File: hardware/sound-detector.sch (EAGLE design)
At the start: 42 parts, among them IC1 LMV324, J1 GATORGATOR_MINI, J2 GATORGATOR_MINI, J3 GATORGATOR_MINI, J4 GATORGATOR_MINI, J5 GATORGATOR_MINI

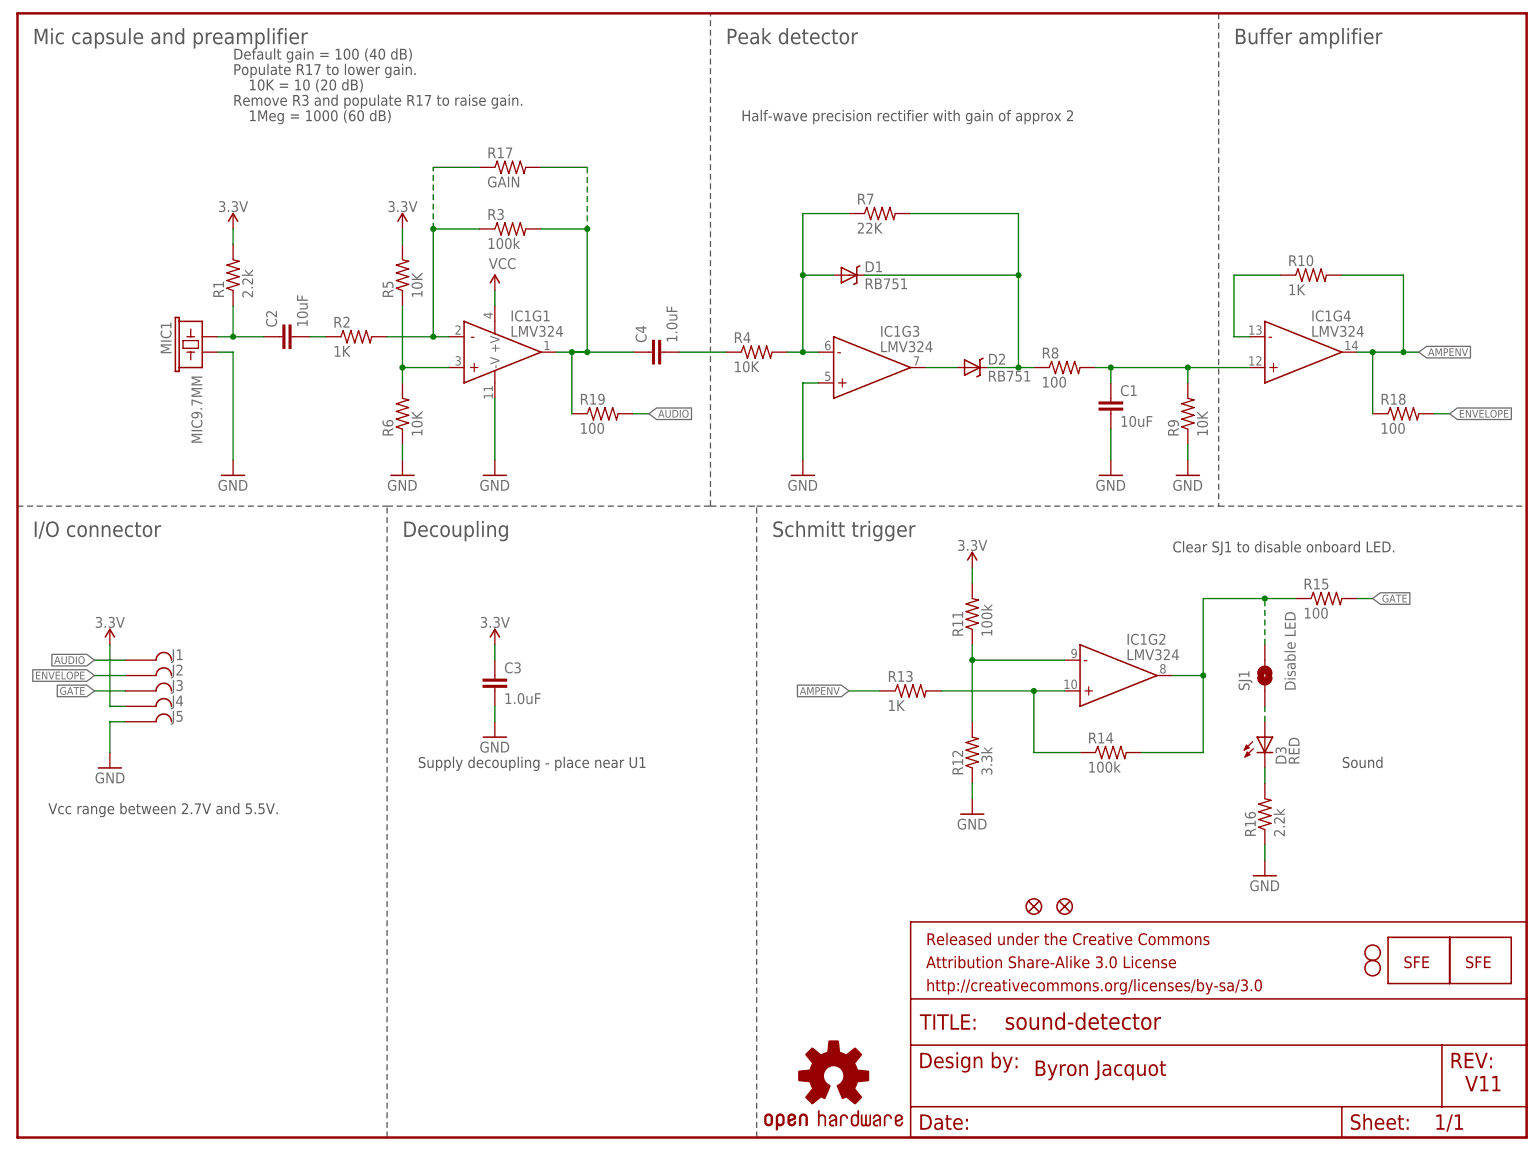
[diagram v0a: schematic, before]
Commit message: adding protection circuitry
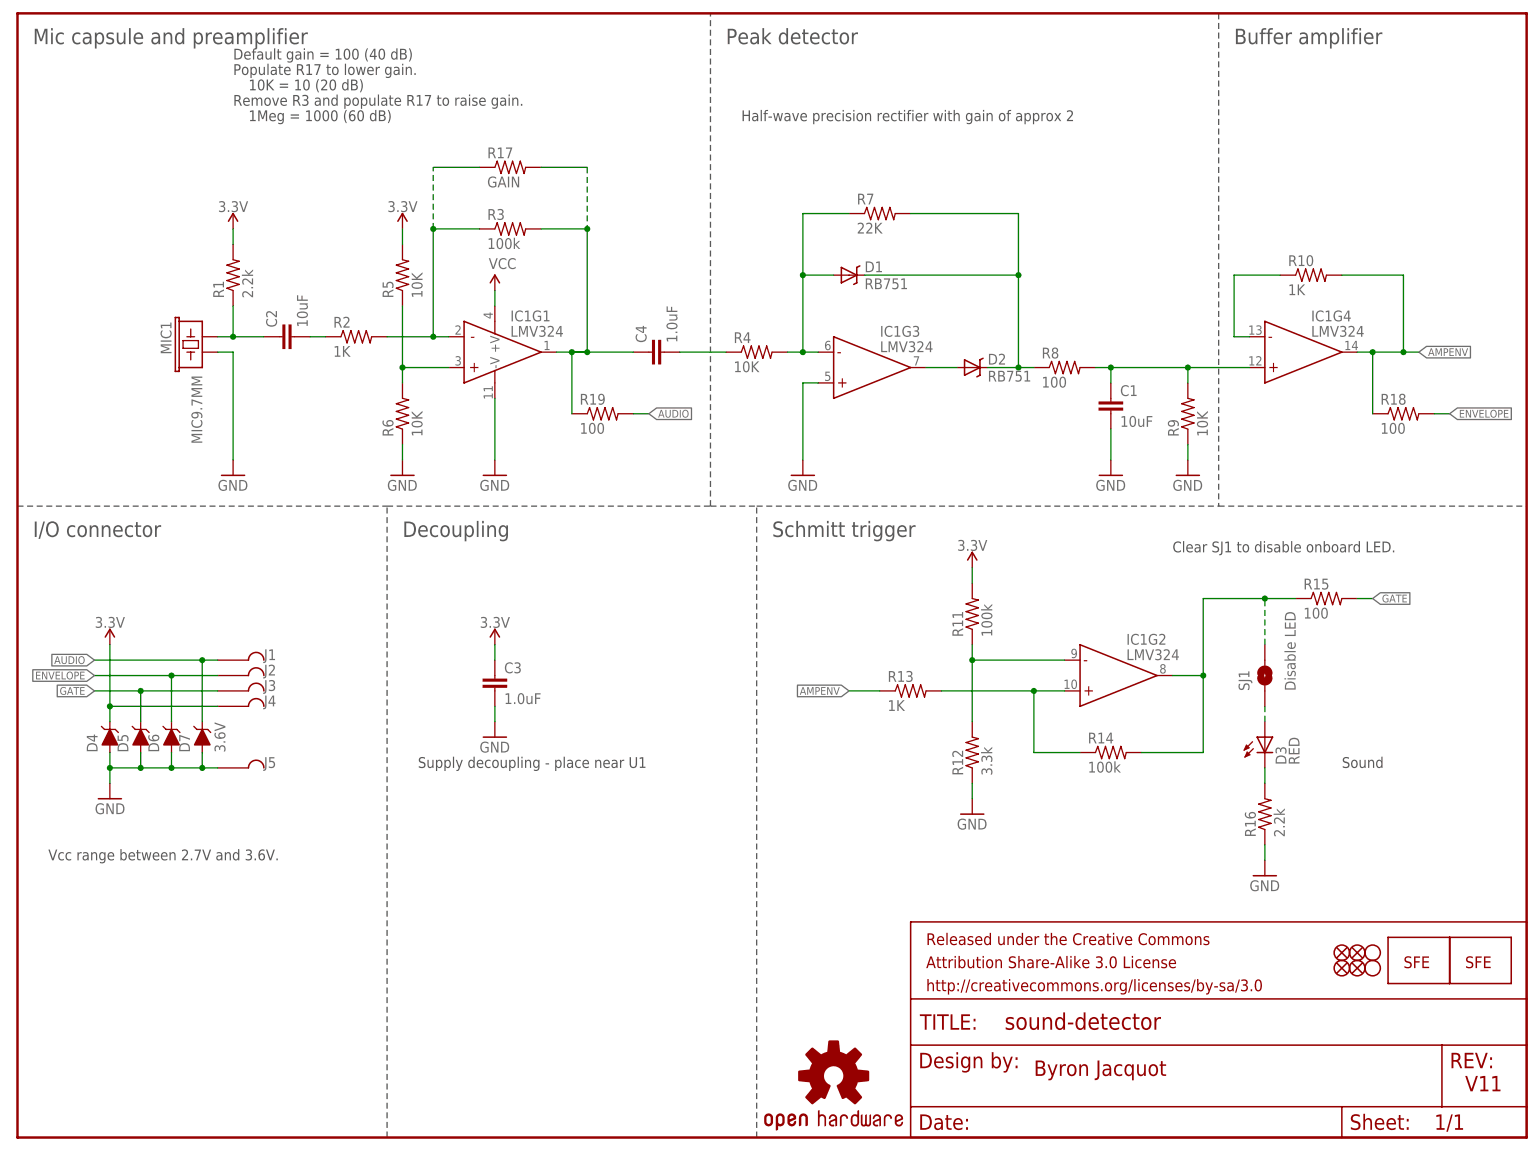
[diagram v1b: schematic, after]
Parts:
- added D4, D5, D6, D7: 3.6V, SparkFun-DiscreteSemi:DIODE-ZENER-BZT52C3V6S
- added FID1, FID2: FIDUCIAL1X2, SparkFun-Aesthetics:FIDUCIAL1X2
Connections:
- net 3.3V: now also D4.C
- net AUDIO: now also D7.C
- net ENVELOPE: now also D6.C
- net GATE: now also D5.C
- net GND: now also D4.A, D5.A, D6.A, D7.A
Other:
- note added: "Vcc range between 2.7V and 3.6V."
- note removed: "Vcc range between 2.7V and 5.5V."
- moved on the sheet: J1, J2, J3, J4, J5

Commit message: initial layout
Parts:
- removed D7: 3.6V, SparkFun-DiscreteSemi:DIODE-ZENER-BZT52C3V6S
- removed SJ1: Disable LED, SparkFun-Passives:SOLDERJUMPERNC
- removed STANDOFF1, STANDOFF2: STAND-OFF, SparkFun-Electromechanical:STAND-OFF
- added J6, J7, J8: GATORGATOR_MINI, SparkFun-Connectors:GATORGATOR_MINI
- added Q1: 2.5A/30V/105mΩ, SparkFun-DiscreteSemi:MOSFET_PCH-DMG2307L
- added R20: 1M, SparkFun-Resistors:1MOHM-0603-1/4W-5%
- added R21, R22, R23: 10k, SparkFun-Resistors:10KOHM-0603-1/10W-1%
- added S1: (no value), SparkFun-Switches:SWITCH-SP3T-SMD
- added U1: ADS1015, SparkFun-IC-Conversion:ADS1015
- C3, C4: device SparkFun-Capacitors:1.0UF-16V-10%(0603) -> SparkFun-Capacitors:1.0UF-0603-16V-10%
- D1, D2: value RB751 -> 120mA/40V/370mV; device SparkFun-DiscreteSemi:RB751 -> SparkFun-DiscreteSemi:DIODE-SCHOTTKY-RB751S40
- LOGO1: value OSHW-LOGOM -> OSHW-LOGOS; device SparkFun-Aesthetics:OSHW-LOGOM -> SparkFun-Aesthetics:OSHW-LOGOS
- LOGO2: value LOGO-SFENW2 -> SFE_LOGO_NAME_FLAME.2_INCH; device SparkFun-Aesthetics:LOGO-SFENW2 -> SparkFun-Aesthetics:SFE_LOGO_NAME_FLAME.2_INCH
- LOGO3: value LOGO-SFESK -> SFE_LOGO_FLAME.2_INCH; device SparkFun-Aesthetics:LOGO-SFESK -> SparkFun-Aesthetics:SFE_LOGO_FLAME.2_INCH
- R1: device SparkFun-Resistors:2.2KOHM1/10W1%(0603) -> SparkFun-Resistors:2.2KOHM-0603-1/10W-1%
- R10, R13, R2: value 1K -> 1k; device SparkFun-Resistors:1KOHM1/10W1%(0603) -> SparkFun-Resistors:1KOHM-0603-1/10W-1%
- R11, R14, R3: device SparkFun-Resistors:100KOHM1/10W1%(0603) -> SparkFun-Resistors:100KOHM-0603-1/10W-1%
- R15, R18, R19, R8: device SparkFun-Resistors:100OHM1/10W1%(0603) -> SparkFun-Resistors:100OHM-0603-1/4W-5%
- R16: value 2.2k -> 1k; device SparkFun-Resistors:2.2KOHM1/10W1%(0603) -> SparkFun-Resistors:1KOHM-0603-1/10W-1%
- R17: value GAIN -> 10k; device SparkFun-Resistors:RESISTORPTH-1/4W-VERT-KIT -> SparkFun-Resistors:10KOHM-0603-1/10W-1%
- R4, R5, R6, R9: value 10K -> 10k; device SparkFun-Resistors:10KOHM1/10W1%(0603)0603 -> SparkFun-Resistors:10KOHM-0603-1/10W-1%
- R7: value 22K -> 22k; device SparkFun-Resistors:22KOHM1/10W1%(0603) -> SparkFun-Resistors:22KOHM-0603-1/10W-1%
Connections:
- removed net N$12: D3.A, SJ1.1
- new net N$13: R17.2, S1.4
- new net N$14: R3.2, S1.2
- new net N$18: R20.2, S1.1
- new net N$19: J4.P$1, J8.P$1, Q1.D
- new net N$20: D4.A, Q1.G, R21.2
- new net SCL: D6.C, J2.P$1, J7.P$1, R23.1, U1.SCL
- new net SDA: D5.C, J3.P$1, J6.P$1, R22.1, U1.SDA
- net 3.3V: now also D3.A, Q1.S, R22.2, R23.2, U1.VDD; no longer J4.P$1
- net AUDIO: now also U1.AIN0; no longer D7.C, J1.P$1
- net ENVELOPE: now also U1.AIN2; no longer D6.C, J2.P$1
- net GATE: now also U1.AIN3; no longer D5.C, J3.P$1
- net GND: now also J1.P$1, R21.1, U1.ADDR, U1.VSS; no longer D4.A, D7.A
- net N$: now also S1.3; no longer R17.2, R3.2
- net N$17: no longer SJ1.2
- net N$4: now also R20.1
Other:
- note added: "ADC-to-I2C"
- note added: "Connections"
- note removed: "Decoupling"
- note removed: "I/O connector"
- note removed: "Supply decoupling - place near U1"
- moved on the sheet: C3, D4, D5, D6, J1, J2, J3, J4, J5, R17, R3

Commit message: post engineer run of checklist
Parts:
- removed IC1: LMV324, SparkFun-AnalogIC:LMV324
- added C5: 0.1uF, SparkFun-Capacitors:0.1UF-0603-25V-(+80/-20%)
- added H1, H2: STAND-OFFTIGHT, SparkFun-Hardware:STAND-OFFTIGHT
- added TP1: TEST-POINT3, SparkFun-Connectors:TEST-POINT3
- added U2: LMV324, SparkFun-IC-Amplifiers:LMV324
- R12: device SparkFun-Resistors:3.3KOHM1/10W1%(0603) -> SparkFun-Resistors:3.3KOHM-0603-1/10W-1%
- R15, R18, R19, R8: device SparkFun-Resistors:100OHM-0603-1/4W-5% -> SparkFun-Resistors:100OHM-0603-1/10W-1%
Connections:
- new net N$12: TP1.1, U1.AIN1
- net 3.3V: now also C5.1, U2G5.P$V+; no longer IC1G1.+V
- net AMPENV: now also U2G4.OUT; no longer IC1G4.OUT
- net GND: now also C5.2, U2G3.+IN, U2G5.P$V-; no longer IC1G1.-V, IC1G3.+IN
- net N$: now also U2G1.OUT; no longer IC1G1.OUT
- net N$10: now also U2G4.+IN; no longer IC1G4.+IN
- net N$11: now also U2G4.-IN; no longer IC1G4.-IN
- net N$15: now also U2G2.-IN; no longer IC1G2.-IN
- net N$16: now also U2G2.+IN; no longer IC1G2.+IN
- net N$17: now also U2G2.OUT; no longer IC1G2.OUT
- net N$2: now also U2G1.+IN; no longer IC1G1.+IN
- net N$4: now also U2G1.-IN; no longer IC1G1.-IN
- net N$7: now also U2G3.-IN; no longer IC1G3.-IN
- net N$8: now also U2G3.OUT; no longer IC1G3.OUT
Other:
- note added: "Address: 0x48"
- note added: "Andrew England"
- note added: "v01"
- note removed: "10K = 10 (20 dB)"
- note removed: "1Meg = 1000 (60 dB)"
- note removed: "Byron Jacquot"
- note removed: "Clear SJ1 to disable onboard LED."
- note removed: "Default gain = 100 (40 dB)"
- note removed: "Populate R17 to lower gain."
- note removed: "Remove R3 and populate R17 to raise gain."
- note removed: "Sound"
- note removed: "V11"
- moved on the sheet: D3, R10, R16, R18, R9, U1
